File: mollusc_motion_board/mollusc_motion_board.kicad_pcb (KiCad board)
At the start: 4 copper layers, 94 x 78.7 mm, 47 parts, among them J2 Barrel_Jack_Switch 12V, J4 RJ45 x4, SW1 SW_Push, SW2 SW_Push, U1 SN74AHCT125N, U2 SN74AHCT125N, U3 SN74AHCT125N, U4 74HC14, U5 Teensy4.0, U6 SN74AHCT125N, U7 74LVC2G241, U8 LM7805_TO220

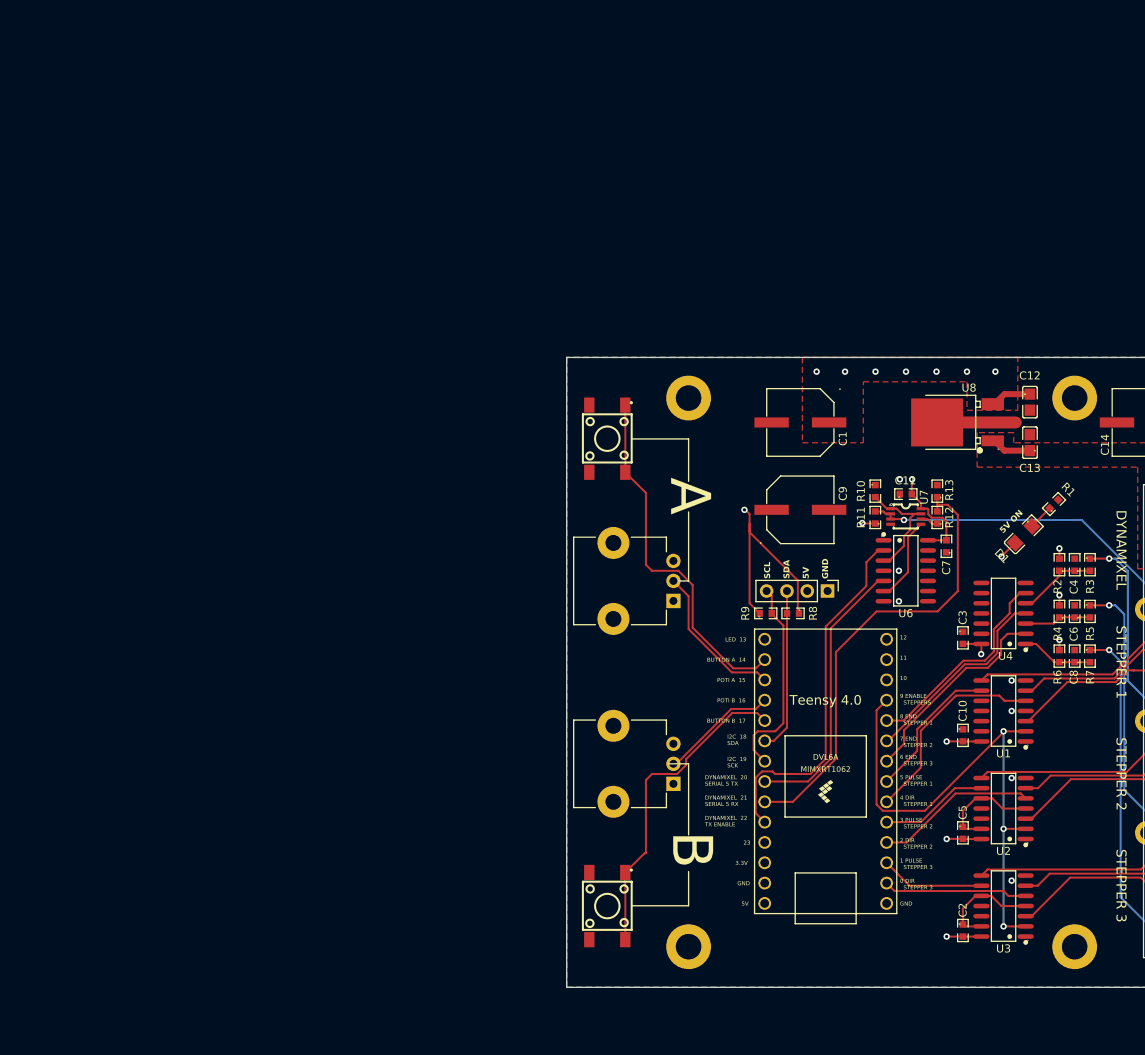
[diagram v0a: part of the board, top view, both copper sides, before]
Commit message: adding BOM
renaming to 'mollusc_motion'
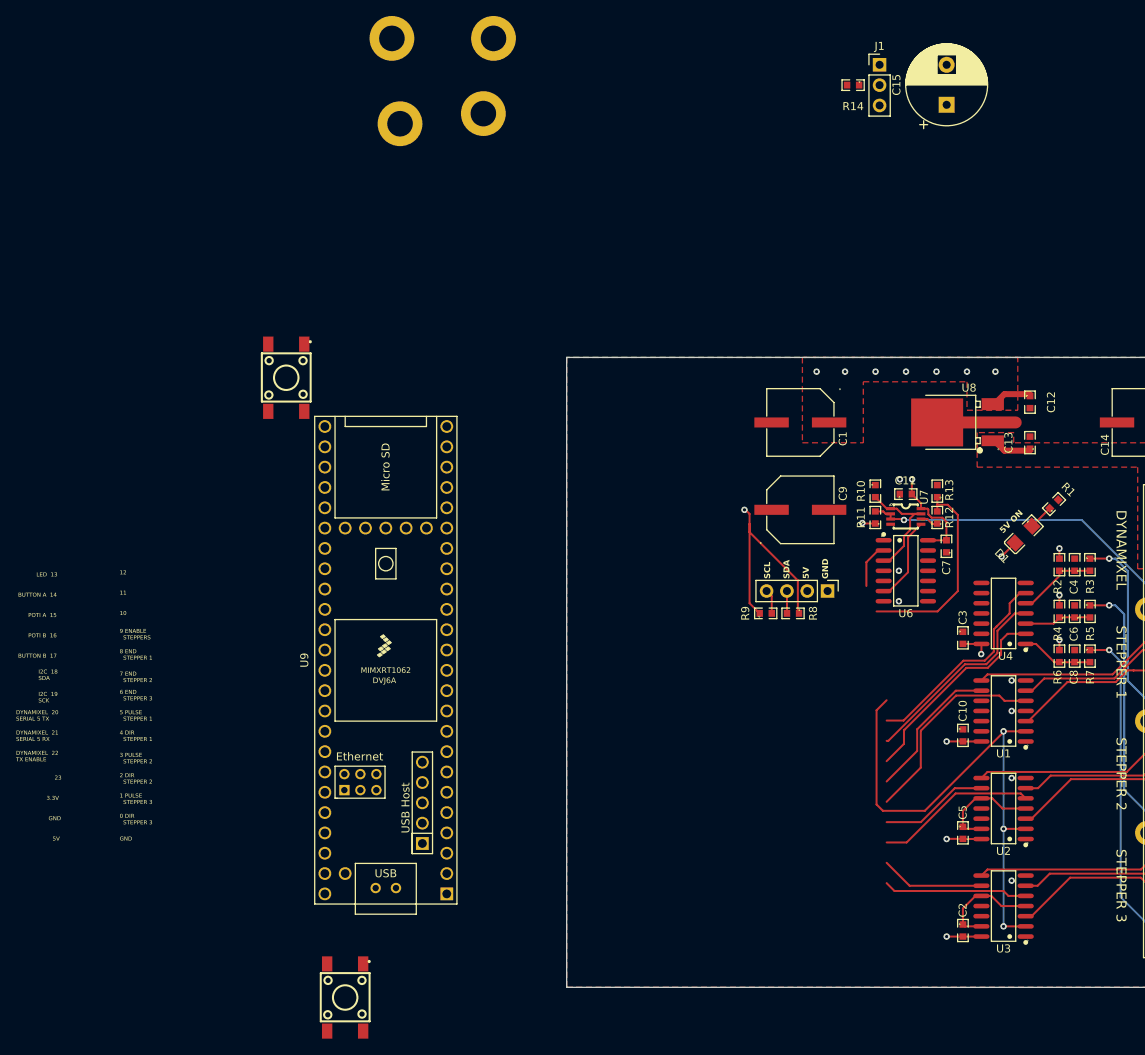
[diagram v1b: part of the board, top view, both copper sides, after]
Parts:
- removed RV1, RV2: R_Potentiometer, Potentiometer_THT:Potentiometer_TT_P0915N
- removed U5: Teensy4.0, teensy:Teensy40
- added C15: 1000uF 25V, Capacitor_THT:CP_Radial_D10.0mm_P5.00mm, F.Cu at (100.8, 39.5)
- added J1: Neopixel Conn., Connector_PinHeader_2.54mm:PinHeader_1x03_P2.54mm_Vertical, F.Cu at (92.5, 34.5)
- added R14: 470, HangOn_Mainboard:R0603, F.Cu at (89.1, 37.1)
- added U9: Teensy4.1, teensy:Teensy41, F.Cu at (30.7, 109.0)
- C12, C13: footprint HangOn_Mainboard:C0805 -> HangOn_Mainboard:R0603
- moved H3 127.7 mm to (42.9, 40.6)
- moved H2 109.0 mm to (32.5, 41.9)
- moved H4 85.4 mm to (44.2, 31.2)
- moved H1 58.3 mm to (31.5, 31.2)
- moved SW2 40.8 mm to (18.3, 73.7)
- moved SW1 34.7 mm to (25.7, 151.1)
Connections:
- net Net-(J_I2C1-Pin_3) renamed /I2C_SCL
- net Net-(J_I2C1-Pin_4) renamed /I2C_SDA
- SW1 pad 1: Net-(U5-17_A3_TX4_SDA1) -> GND
- SW1 pad 2: GND -> Net-(U9-17_A3_TX4_SDA1)
- SW2 pad 1: Net-(U5-14_A0_TX3_SPDIF_OUT) -> GND
- SW2 pad 2: GND -> Net-(U9-14_A0_TX3_SPDIF_OUT)
- U6 pad 2: /DYN_TX_ENABLE -> /DYN_DIRECTION
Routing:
- net /DYN_TX_ENABLE: track 45.5 -> 0.00 mm
- net Net-(U5-14_A0_TX3_SPDIF_OUT): track 44.8 -> 0.00 mm
- net Net-(U5-17_A3_TX4_SDA1): track 40.3 -> 0.00 mm
- net /DYN_TX: track 34.8 -> 0.70 mm
- net /DYN_RX: track 57.3 -> 25.6 mm
- net /I2C_SDA: track 25.5 -> 3.06 mm
- net Net-(U5-15_A1_RX3_SPDIF_IN): track 19.0 -> 0.00 mm
- net /I2C_SCL: track 21.4 -> 2.80 mm
- net Net-(U5-16_A2_RX4_SCL1): track 14.7 -> 0.00 mm
- net /DYN_DIRECTION: track 0.00 -> 5.75 mm
- added copper zone on In1.Cu, net GND
- removed copper zone on In1.Cu, net +5V
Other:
- board text removed: "A"
- board text removed: "B"

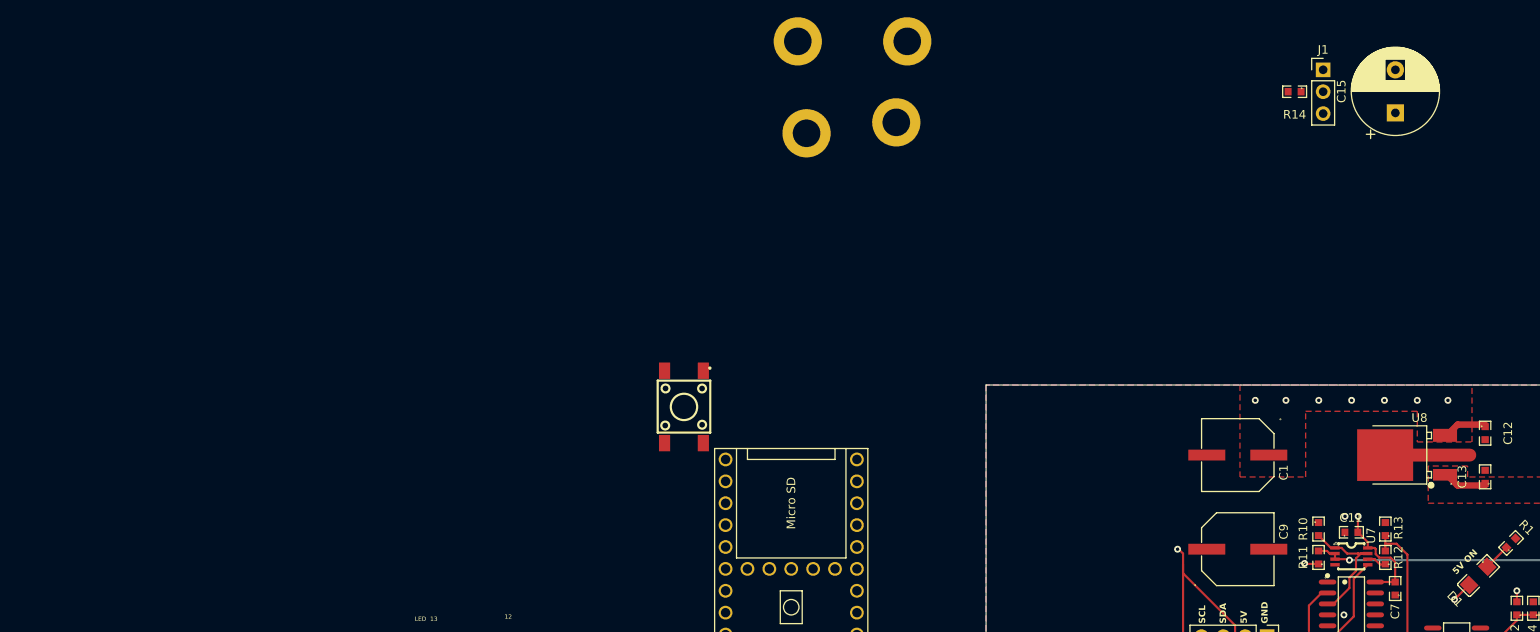
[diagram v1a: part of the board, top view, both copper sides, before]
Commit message: adding ethernet jack
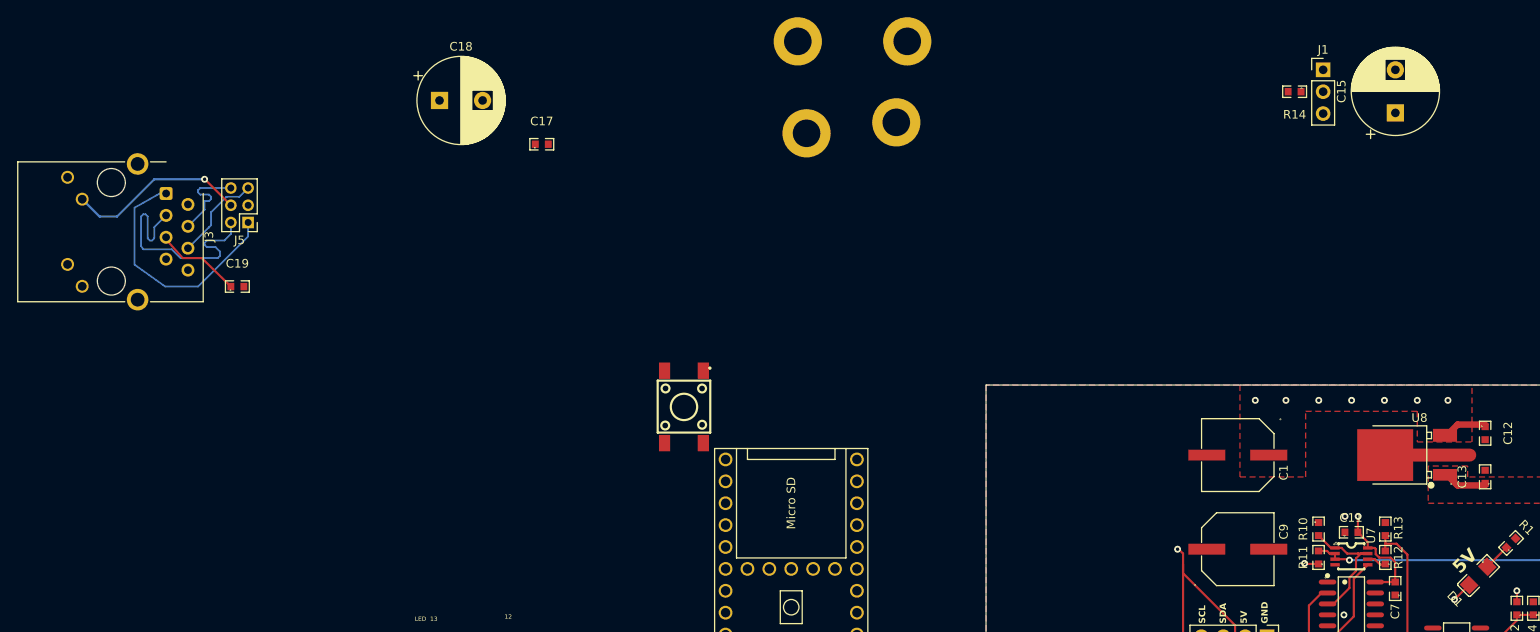
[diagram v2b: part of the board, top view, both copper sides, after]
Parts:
- added C17: 0.1uF 16V, HangOn_Mainboard:R0603, F.Cu at (1.79, 43.2)
- added C18: 500uF 25V, Capacitor_THT:CP_Radial_D10.0mm_P5.00mm, F.Cu at (-10.1, 38.1)
- added C19: 0.1uF 35V, HangOn_Mainboard:R0603, F.Cu at (-33.5, 59.7)
- added J3: RJ45_LED_Shielded, Connector_RJ:RJ45_Cetus_J1B1211CCD_Horizontal, F.Cu at (-41.8, 48.9)
- added J5: Conn_01x06_Pin, Connector_PinHeader_2.00mm:PinHeader_2x03_P2.00mm_Vertical, F.Cu at (-32.3, 52.3)
- C15: value 1000uF 25V -> 500uF 25V
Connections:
- J4 pad D7: +12V -> GND
- J4 pad D8: +12V -> GND
- U9 pad 16: unconnected-(U9-24_A10_TX6_SCL2-Pad16) -> /NEOPIXEL_SIG
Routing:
- net /ETH_TX+: track 0.00 -> 28.7 mm
- net /ETH_TX-: track 0.00 -> 28.7 mm
- net Net-(J5-Pin_4): track 0.00 -> 21.1 mm, vias 0 -> 1
- net /ETH_RX-: track 0.00 -> 10.8 mm
- net /ETH_RX+: track 0.00 -> 10.7 mm
- net Net-(C19-Pad1): track 0.00 -> 10.1 mm
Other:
- board text removed: "5V ON"

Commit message: Board v2 wip
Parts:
- removed U8: LM7805_TO220, HangOn_Mainboard:TO-252-2_L6.5-W6.1-P4.58-LS10.0-TL
- added BT1: Battery_Cell, molluscmotion:BAT_S8421-45R, F.Cu at (129.5, 54.6)
- added C16: 110uF 35V, molluscmotion:CAP-SMD_BD6.3-L6.6-W6.6-LS7.2-FD, F.Cu at (165.7, 121.3)
- added D2: LED, molluscmotion:LED0603-RD, F.Cu at (137.2, 132.1)
- added D3: SMAJ14A_C908768, molluscmotion:SMA_L4.3-W2.6-LS5.1-RD, F.Cu at (122.5, 147.6)
- added J6: D36V50F5, clockdiv:Pololu_5V_5.5A_Step-Down_Voltage_Regulator_D36V50F5, F.Cu at (128.2, 141.0)
- added J7: Endswitches Test Conn, Connector_PinHeader_2.54mm:PinHeader_1x03_P2.54mm_Vertical, F.Cu at (137.4, 106.8)
- added R15: 510, molluscmotion:R0603, F.Cu at (135.3, 132.1)
- added TP1: TP12V, TestPoint:TestPoint_THTPad_2.5x2.5mm_Drill1.2mm, F.Cu at (146.0, 132.1)
- added TP2: TPGND, TestPoint:TestPoint_THTPad_2.5x2.5mm_Drill1.2mm, F.Cu at (146.0, 138.4)
- added TP3: TP5V, TestPoint:TestPoint_THTPad_2.5x2.5mm_Drill1.2mm, F.Cu at (146.1, 125.7)
- added TP4: TP3V3, TestPoint:TestPoint_THTPad_2.5x2.5mm_Drill1.2mm, F.Cu at (146.0, 119.4)
- C1, C9: footprint HangOn_Mainboard:CAP-SMD_BD8.0-L8.3-W8.3-LS9.9-FD -> molluscmotion:CAP-SMD_BD8.0-L8.3-W8.3-LS9.9-FD
- C10, C11, C17, C2, C3, C4, C5, C6, C7, C8: value 0.1uF 16V -> 0.1uF 50V; footprint HangOn_Mainboard:R0603 -> molluscmotion:C0603
- C12: value 0.1uF 35V -> 220uF 35V; footprint HangOn_Mainboard:R0603 -> molluscmotion:CAP-SMD_BD8.0-L8.3-W8.3-LS9.9-FD
- C13: value 0.33uF 35V -> 220uF 35V; footprint HangOn_Mainboard:R0603 -> molluscmotion:CAP-SMD_BD8.0-L8.3-W8.3-LS9.9-FD
- C14: value 220uF 35V -> 110uF 35V; footprint HangOn_Mainboard:CAP-SMD_BD8.0-L8.3-W8.3-LS9.9-FD -> molluscmotion:CAP-SMD_BD6.3-L6.6-W6.6-LS7.2-FD
- C15, C18: value 500uF 25V -> 1000uF 25V
- C19: value 0.1uF 35V -> 0.1uF 50V; footprint HangOn_Mainboard:R0603 -> molluscmotion:C0603
- D1: footprint HangOn_Mainboard:LED1206-R-RD_WHITE -> molluscmotion:LED0603-RD
- H1, H2, H3, H4: footprint MountingHole:MountingHole_3.2mm_M3_DIN965_Pad -> MountingHole:MountingHole_3.2mm_M3_DIN965_Pad_TopBottom
- R1: value 470 -> 220; footprint HangOn_Mainboard:R0603 -> molluscmotion:R0603
- R10, R11, R12, R13, R14, R2, R3, R4, R5, R6, R7, R8, R9: footprint HangOn_Mainboard:R0603 -> molluscmotion:R0603
- SW1, SW2: footprint HangOn_Mainboard:KEY-SMD_4P-L6.1-W6.1-P4.50-LS9.0 -> molluscmotion:KEY-SMD_4P-L6.1-W6.1-P4.50-LS9.0
- U1, U2, U3, U4, U6: footprint HangOn_Mainboard:SOIC-14_L8.7-W3.9-P1.27-LS6.0-BL -> molluscmotion:SOIC-14_L8.7-W3.9-P1.27-LS6.0-BL
- U7: footprint HangOn_Mainboard:SSOP-8_L3.0-W2.8-P0.65-LS4.0-BL -> molluscmotion:SSOP-8_L3.0-W2.8-P0.65-LS4.0-BL
- moved C17 186.2 mm to (170.8, 121.3), turned to 90 degrees
- moved C19 157.9 mm to (109.0, 127.7), turned to 45 degrees
- moved J3 157.4 mm to (95.5, 125.9), turned to -45 degrees
- moved J5 153.4 mm to (104.6, 121.6), turned to -135 degrees
- moved SW1 126.0 mm to (78.7, 36.8)
- moved C18 113.4 mm to (97.8, 73.0), turned to -135 degrees
- moved C9 85.8 mm to (165.1, 66.7), turned to 180 degrees
- moved C12 79.7 mm to (142.8, 149.8)
- moved U9 72.8 mm to (102.9, 99.1), turned to 0 degrees
- moved H1 71.3 mm to (-39.4, 23.0)
- moved H2 71.3 mm to (-38.4, 33.7)
- moved H3 71.3 mm to (-27.9, 32.4)
- moved H4 71.3 mm to (-26.7, 23.0)
- moved C11 70.5 mm to (36.0, 125.7)
- moved U7 70.5 mm to (36.0, 128.5)
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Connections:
- C12 pad 1: +5V -> /Vin
- C13 pad 1: +12V -> +5V
- J2 pad 1: +12V -> /Vin
- J4 pad A1: /Stepper03/SIG -> /DynamixelConnection/DYN_DATA
- J4 pad A3: +3.3V -> +12V
- J4 pad A4: /Stepper03/ENA+ -> +12V
- J4 pad A5: GND -> +12V
- J4 pad A6: /Stepper03/DIR+ -> +12V
- J4 pad A8: /Stepper03/PUL+ -> GND
- J4 pad B1: /Stepper02/SIG -> /Stepper03/SIG
- J4 pad B4: /Stepper02/ENA+ -> /Stepper03/ENA+
- J4 pad B6: /Stepper02/DIR+ -> /Stepper03/DIR+
- J4 pad B8: /Stepper02/PUL+ -> /Stepper03/PUL+
- J4 pad C1: /Stepper01/SIG -> /Stepper02/SIG
- J4 pad C4: /Stepper01/ENA+ -> /Stepper02/ENA+
- J4 pad C6: /Stepper01/DIR+ -> /Stepper02/DIR+
- J4 pad C8: /Stepper01/PUL+ -> /Stepper02/PUL+
- J4 pad D1: /DynamixelConnection/DYN_DATA -> /Stepper01/SIG
- J4 pad D3: +12V -> +3.3V
- J4 pad D4: +12V -> /Stepper01/ENA+
- J4 pad D5: +12V -> GND
- J4 pad D6: +12V -> /Stepper01/DIR+
- J4 pad D8: GND -> /Stepper01/PUL+
- U9 pad 10: /STEPPER_01_END -> /STEPPER_03_END
- U9 pad 50: unconnected-(U9-VBAT-Pad50) -> Net-(BT1-+)
- U9 pad 52: unconnected-(U9-GND-Pad52) -> Net-(BT1--)
- U9 pad 8: /STEPPER_03_END -> /STEPPER_01_END
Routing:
- net +3.3V: track 269.5 -> 67.0 mm, vias 5 -> 3
- net /Stepper03/SIG: track 42.7 -> 0.00 mm, vias 1 -> 0
- net /DynamixelConnection/DYN_DATA: track 42.2 -> 2.68 mm, vias 1 -> 0
- net /Stepper02/SIG: track 34.8 -> 0.00 mm, vias 1 -> 0
- net /NEOPIXEL_SIG: track 0.00 -> 30.6 mm, vias 0 -> 1
- net +5V: track 34.6 -> 63.4 mm, vias 13 -> 5
- net /TEENSY_STEPPER_ENABLE: track 66.6 -> 94.7 mm
- net /Stepper01/SIG: track 26.3 -> 0.00 mm, vias 1 -> 0
- net /STEPPER_01_DIR: track 25.9 -> 0.00 mm
- net /Stepper01/PUL+: track 24.6 -> 0.00 mm
- net /Stepper02/PUL+: track 23.9 -> 0.00 mm
- net /Stepper03/PUL+: track 23.1 -> 0.00 mm
- net /STEPPER_02_DIR: track 20.2 -> 0.00 mm
- net /Stepper03/ENA+: track 19.3 -> 0.00 mm
- net /Stepper01/ENA+: track 19.1 -> 0.00 mm
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- removed copper zone on F.Cu, net +12V
- removed copper zone on In1.Cu, net +12V
- removed copper zone on F.Cu, net +5V
- removed copper zone on B.Cu, net GND
- removed copper zone on F.Cu, net GND
- removed copper zone on In1.Cu, net GND
- removed copper zone on In2.Cu, net GND
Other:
- board size 94 x 78.7 mm -> 120 x 120 mm
- board text added: "3V3"
- board text added: "VIn"

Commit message: PCB v1.2 Layout
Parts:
- added C20: 220uF 35V, molluscmotion:CAP-SMD_BD8.0-L8.3-W8.3-LS9.9-FD, F.Cu at (166.8, 60.7)
- added D4: ESD5Z5_0T1G, molluscmotion:SOD-523F_L1.2-W0.8-LS1.7-RD, F.Cu at (128.5, 64.4)
- added D5: ESD5Z5_0T1G, molluscmotion:SOD-523F_L1.2-W0.8-LS1.7-RD, F.Cu at (114.6, 64.3)
- added D6: ESD5Z5_0T1G, molluscmotion:SOD-523F_L1.2-W0.8-LS1.7-RD, F.Cu at (142.5, 64.3)
- C14: value 110uF 35V -> 220uF 35V; footprint molluscmotion:CAP-SMD_BD6.3-L6.6-W6.6-LS7.2-FD -> molluscmotion:CAP-SMD_BD8.0-L8.3-W8.3-LS9.9-FD
- C16: value 110uF 35V -> 0.1uF 50V; footprint molluscmotion:CAP-SMD_BD6.3-L6.6-W6.6-LS7.2-FD -> molluscmotion:C0603
- TP1, TP2, TP3, TP4: footprint TestPoint:TestPoint_THTPad_2.5x2.5mm_Drill1.2mm -> TestPoint:TestPoint_THTPad_1.5x1.5mm_Drill0.7mm
- moved R10 136.9 mm to (157.8, 70.8), turned to 180 degrees
- moved R11 135.2 mm to (154.5, 70.8), turned to 0 degrees
- moved C11 131.7 mm to (157.4, 74.7), turned to -90 degrees
- moved U7 130.2 mm to (154.6, 74.7), turned to 180 degrees
- moved U6 127.2 mm to (147.9, 74.7), turned to 180 degrees
- moved R13 126.8 mm to (157.8, 78.6), turned to 0 degrees
- moved R12 125.0 mm to (154.5, 78.6), turned to 0 degrees
- moved C7 121.7 mm to (150.9, 79.7), turned to 0 degrees
- moved J_I2C1 111.4 mm to (116.8, 141.0), turned to 180 degrees
- moved SW1 110.8 mm to (100.3, 145.5), turned to -45 degrees
- moved R9 109.1 mm to (113.7, 133.3)
- moved R8 107.8 mm to (113.7, 136.0), turned to 0 degrees
- moved SW2 83.1 mm to (81.9, 127.0), turned to -45 degrees
- moved C12 75.3 mm to (180.3, 84.5), turned to 0 degrees
- moved C1 73.8 mm to (114.3, 149.9), turned to 90 degrees
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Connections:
- BT1 pad 1: Net-(BT1-+) -> /BAT+
- BT1 pad 2: Net-(BT1--) -> /BAT-
- C16 pad 1: +12V -> /BAT+
- C16 pad 2: GND -> /BAT-
- SW2 pad 2: Net-(U9-14_A0_TX3_SPDIF_OUT) -> Net-(U9-16_A2_RX4_SCL1)
- U9 pad 36: Net-(U9-14_A0_TX3_SPDIF_OUT) -> unconnected-(U9-14_A0_TX3_SPDIF_OUT-Pad36)
- U9 pad 38: unconnected-(U9-16_A2_RX4_SCL1-Pad38) -> Net-(U9-16_A2_RX4_SCL1)
- U9 pad 50: Net-(BT1-+) -> /BAT+
- U9 pad 52: Net-(BT1--) -> /BAT-
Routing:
- net +5V: track 63.4 -> 368.9 mm, vias 5 -> 9
- net +3.3V: track 67.0 -> 257.2 mm, vias 3 -> 6
- net /DYN_DIRECTION: track 0.00 -> 100.9 mm, vias 0 -> 2
- net /STEPPER_01_DIR: track 0.00 -> 99.4 mm, vias 0 -> 1
- net /DYN_TX: track 0.70 -> 94.0 mm
- net /STEPPER_02_DIR: track 0.00 -> 93.0 mm, vias 0 -> 1
- net /STEPPER_01_PULSE: track 0.00 -> 90.8 mm, vias 0 -> 1
- net /STEPPER_03_DIR: track 0.00 -> 87.1 mm, vias 0 -> 1
- net /STEPPER_02_PULSE: track 0.00 -> 84.5 mm, vias 0 -> 1
- net /BAT-: track 0.00 -> 82.9 mm, vias 0 -> 5
- net /BAT+: track 0.00 -> 80.6 mm, vias 0 -> 5
- net /STEPPER_03_PULSE: track 0.00 -> 78.5 mm, vias 0 -> 1
- net /DYN_RX: track 25.6 -> 92.9 mm
- net /Vin: track 0.00 -> 54.0 mm
- net Net-(D6-C): track 3.81 -> 57.6 mm
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- added copper zone on F.Cu, net +12V
- added copper zone on B.Cu, net GND
- added copper zone on F.Cu, net GND
- added copper zone on In1.Cu, net GND
- added copper zone on In2.Cu, net GND
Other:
- outline, holes or cut-outs redrawn
- board text removed: "DYNAMIXEL"
- board text removed: "STEPPER 1"
- board text removed: "STEPPER 2"
- board text removed: "STEPPER 3"
